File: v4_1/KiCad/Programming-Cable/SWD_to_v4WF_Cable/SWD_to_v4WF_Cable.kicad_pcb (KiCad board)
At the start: 2 copper layers, 60 x 20 mm, 19 parts, among them J1 Conn_01x05, J2 Conn_02x05_Odd_Even

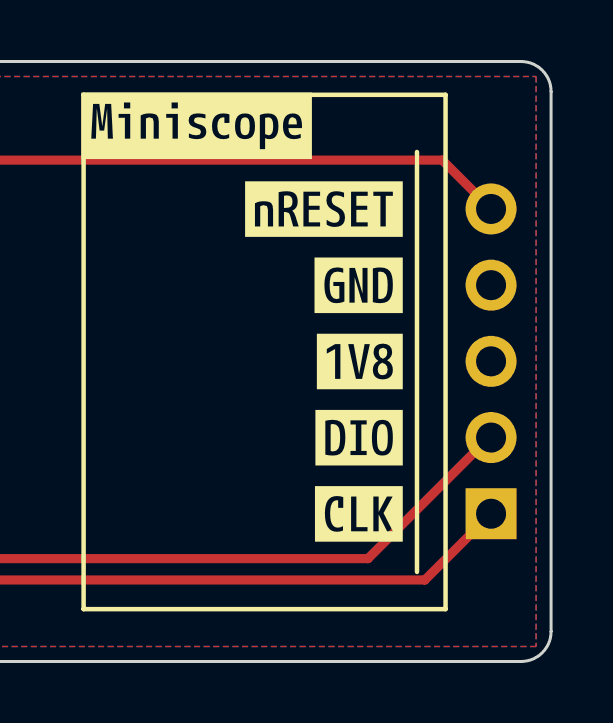
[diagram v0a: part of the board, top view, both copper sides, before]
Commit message: Modification to the Programming cable PCB and firmware
- Corrected the footprint and layout of the programming cable PCB. Switched from a 100 mil pogo pin connector to the correct size (50 mil)
- Cleaned and built the firmware for flashing to the MCU
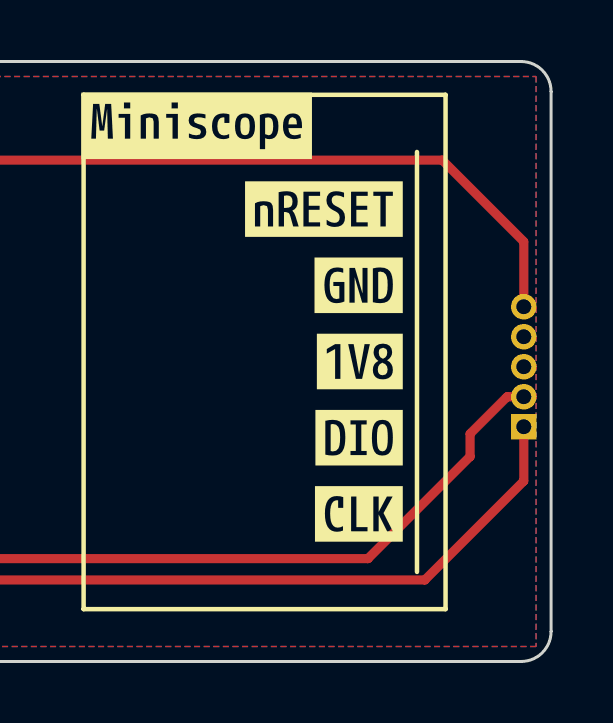
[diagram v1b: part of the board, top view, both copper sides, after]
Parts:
- J1: footprint Connector_PinHeader_2.54mm:PinHeader_1x05_P2.54mm_Vertical -> Connector_PinSocket_1.00mm:PinSocket_1x05_P1.00mm_Vertical
- moved J1 3.10 mm to (184.7, 61.5)
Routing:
- net /nRST: track 55.2 -> 59.0 mm
- net /SWDCLK: track 60.9 -> 64.2 mm
- net /SWDIO: track 56.3 -> 58.4 mm
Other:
- board text added: "SWD_to_v4WF_Cable v0.1 Karina Keus and Federico Sangiuliano Aharoni Lab, UCLA 08-31-2022 Rev1 12-3-2022"
- board text removed: "SWD_to_v4WF_Cable v0.1 Karina Keus and Federico Sangiuliano Aharoni Lab, UCLA 08-31-2022"
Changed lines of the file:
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@@
     )
   )
-  (footprint "Connector_PinHeader_2.54mm:PinHeader_1x05_P2.54mm_Vertical" (layer "B.Cu")
-    (at 183.6 64.425)
-    (descr "Through hole straight pin header, 1x05, 2.54mm pitch, single row")
-    (tags "Through hole pin header THT 1x05 2.54mm single row")
+  (footprint "Connector_PinSocket_1.00mm:PinSocket_1x05_P1.00mm_Vertical" (layer "B.Cu")
+    (at 184.69 61.525)
+    (descr "Through hole straight socket strip, 1x05, 1.00mm pitch, single row (https://gct.co/files/drawings/bc065.pdf), script generated")
+    (tags "Through hole socket strip THT 1x05 1.00mm single row")
     (property "Sheetfile" "SWD_to_v4WF_Cable.kicad_sch")
     (property "Sheetname" "")
     (attr through_hole)
-    (fp_text reference "J1" (at 0 2.33) (layer "B.SilkS") hide
+    (fp_text reference "J1" (at -0.29 2.25 180) (layer "B.SilkS")
       (effects (font (size 1 1) (thickness 0.15)) (justify mirror))
     )
-    (fp_text value "Conn_01x05" (at 0 -12.49) (layer "B.Fab")
+    (fp_text value "Conn_01x05" (at -0.29 -6.25 180) (layer "B.Fab")
       (effects (font (size 1 1) (thickness 0.15)) (justify mirror))
     )
-    (fp_text user "${REFERENCE}" (at 0 -5.08 90) (layer "B.Fab")
-      (effects (font (size 1 1) (thickness 0.15)) (justify mirror))
+    (fp_text user "${REFERENCE}" (at -0.29 -2 270) (layer "B.Fab")
+      (effects (font (size 0.9 0.9) (thickness 0.14)) (justify mirror))
     )
-    (fp_line (start 1.33 -1.27) (end 1.33 -11.49) (layer "B.SilkS") (width 0.12))
-    (fp_line (start -1.33 -1.27) (end 1.33 -1.27) (layer "B.SilkS") (width 0.12))
-    (fp_line (start -1.33 1.33) (end 0 1.33) (layer "B.SilkS") (width 0.12))
-    (fp_line (start -1.33 -1.27) (end -1.33 -11.49) (layer "B.SilkS") (width 0.12))
-    (fp_line (start -1.33 0) (end -1.33 1.33) (layer "B.SilkS") (width 0.12))
-    (fp_line (start -1.33 -11.49) (end 1.33 -11.49) (layer "B.SilkS") (width 0.12))
-    (fp_line (start -1.8 1.8) (end -1.8 -11.95) (layer "B.CrtYd") (width 0.05))
-    (fp_line (start 1.8 1.8) (end -1.8 1.8) (layer "B.CrtYd") (width 0.05))
-    (fp_line (start -1.8 -11.95) (end 1.8 -11.95) (layer "B.CrtYd") (width 0.05))
-    (fp_line (start 1.8 -11.95) (end 1.8 1.8) (layer "B.CrtYd") (width 0.05))
-    (fp_line (start -1.27 0.635) (end -0.635 1.27) (layer "B.Fab") (width 0.1))
-    (fp_line (start -1.27 -11.43) (end -1.27 0.635) (layer "B.Fab") (width 0.1))
-    (fp_line (start -0.635 1.27) (end 1.27 1.27) (layer "B.Fab") (width 0.1))
-    (fp_line (start 1.27 1.27) (end 1.27 -11.43) (layer "B.Fab") (width 0.1))
-    (fp_line (start 1.27 -11.43) (end -1.27 -11.43) (layer "B.Fab") (width 0.1))
-    (pad "1" thru_hole rect (at 0 0) (size 1.7 1.7) (drill 1) (layers *.Cu *.Mask)
+    (fp_line (start 0 0.81) (end 0.685 0.81) (layer "B.SilkS") (width 0.12))
+    (fp_line (start 0.52 -4.445898) (end 0.52 -4.81) (layer "B.SilkS") (width 0.12))
+    (fp_line (start 0.685 0.81) (end 0.685 0) (layer "B.SilkS") (width 0.12))
+    (fp_line (start -1.1 -4.81) (end 0.52 -4.81) (layer "B.SilkS") (width 0.12))
+    (fp_line (start 0.52 -3.445898) (end 0.52 -3.554102) (layer "B.SilkS") (width 0.12))
+    (fp_line (start -1.1 -0.5) (end -0.685 -0.5) (layer "B.SilkS") (width 0.12))
+    (fp_line (start 0.52 -1.445898) (end 0.52 -1.554102) (layer "B.SilkS") (width 0.12))
+    (fp_line (start 0.52 -2.445898) (end 0.52 -2.554102) (layer "B.SilkS") (width 0.12))
+    (fp_line (start -1.1 -0.5) (end -1.1 -4.81) (layer "B.SilkS") (width 0.12))
+    (fp_line (start -1.54 1.25) (end 0.96 1.25) (layer "B.CrtYd") (width 0.05))
+    (fp_line (start -1.54 -5.25) (end -1.54 1.25) (layer "B.CrtYd") (width 0.05))
+    (fp_line (start 0.96 1.25) (end 0.96 -5.25) (layer "B.CrtYd") (width 0.05))
+    (fp_line (start 0.96 -5.25) (end -1.54 -5.25) (layer "B.CrtYd") (width 0.05))
+    (fp_line (start 0.46 0.375) (end 0.46 -4.75) (layer "B.Fab") (width 0.1))
+    (fp_line (start 0.085 0.75) (end 0.46 0.375) (layer "B.Fab") (width 0.1))
+    (fp_line (start -1.04 -4.75) (end -1.04 0.75) (layer "B.Fab") (width 0.1))
+    (fp_line (start 0.46 -4.75) (end -1.04 -4.75) (layer "B.Fab") (width 0.1))
+    (fp_line (start -1.04 0.75) (end 0.085 0.75) (layer "B.Fab") (width 0.1))
+    (pad "1" thru_hole rect (at 0 0) (size 0.85 0.85) (drill 0.5) (layers *.Cu *.Mask)
       (net 1 "/SWDCLK") (pinfunction "Pin_1") (pintype "passive"))
-    (pad "2" thru_hole oval (at 0 -2.54) (size 1.7 1.7) (drill 1) (layers *.Cu *.Mask)
+    (pad "2" thru_hole oval (at 0 -1) (size 0.85 0.85) (drill 0.5) (layers *.Cu *.Mask)
       (net 2 "/SWDIO") (pinfunction "Pin_2") (pintype "passive"))
-    (pad "3" thru_hole oval (at 0 -5.08) (size 1.7 1.7) (drill 1) (layers *.Cu *.Mask)
+    (pad "3" thru_hole oval (at 0 -2) (size 0.85 0.85) (drill 0.5) (layers *.Cu *.Mask)
       (net 3 "+1V8") (pinfunction "Pin_3") (pintype "passive"))
-    (pad "4" thru_hole oval (at 0 -7.62) (size 1.7 1.7) (drill 1) (layers *.Cu *.Mask)
+    (pad "4" thru_hole oval (at 0 -3) (size 0.85 0.85) (drill 0.5) (layers *.Cu *.Mask)
       (net 4 "GND") (pinfunction "Pin_4") (pintype "passive"))
-    (pad "5" thru_hole oval (at 0 -10.16) (size 1.7 1.7) (drill 1) (layers *.Cu *.Mask)
+    (pad "5" thru_hole oval (at 0 -4) (size 0.85 0.85) (drill 0.5) (layers *.Cu *.Mask)
       (net 5 "/nRST") (pinfunction "Pin_5") (pintype "passive"))
-    (model "${KICAD6_3DMODEL_DIR}/Connector_PinHeader_2.54mm.3dshapes/PinHeader_1x05_P2.54mm_Vertical.wrl"
+    (model "${KICAD6_3DMODEL_DIR}/Connector_PinSocket_1.00mm.3dshapes/PinSocket_1x05_P1.00mm_Vertical.wrl"
       (offset (xyz 0 0 0))
       (scale (xyz 1 1 1))
@@
   (gr_line (start 185.6 68.35) (end 185.6 50.35) (layer "Edge.Cuts") (width 0.1))
   (gr_arc (start 126.87 69.35) (mid 125.971974 68.978026) (end 125.6 68.08) (layer "Edge.Cuts") (width 0.1))
-  (gr_text "SWD_to_v4WF_Cable v0.1\nKarina Keus and Federico Sangiuliano\nAharoni Lab, UCLA\n08-31-2022" (at 155.729991 59.349996) (layer "B.SilkS")
+  (gr_text "SWD_to_v4WF_Cable v0.1\nKarina Keus and Federico Sangiuliano\nAharoni Lab, UCLA\n08-31-2022\nRev1 12-3-2022" (at 155.729991 59.349996) (layer "B.SilkS")
     (effects (font (size 1 1) (thickness 0.15)) (justify mirror))
   )
+  (segment (start 128.1908 63.3048) (end 128.1908 65.1082) (width 0.3048) (layer "F.Cu") (net 1))
+  (segment (start 129.6106 61.885) (end 128.1908 63.3048) (width 0.3048) (layer "F.Cu") (net 1))
+  (segment (start 184.69 63.335) (end 184.69 61.525) (width 0.3048) (layer "F.Cu") (net 1))
   (segment (start 128.1908 65.1082) (end 129.7148 66.6322) (width 0.3048) (layer "F.Cu") (net 1))
+  (segment (start 181.3928 66.6322) (end 184.69 63.335) (width 0.3048) (layer "F.Cu") (net 1))
+  (segment (start 129.7148 66.6322) (end 181.3928 66.6322) (width 0.3048) (layer "F.Cu") (net 1))
   (segment (start 129.71 61.885) (end 129.6106 61.885) (width 0.3048) (layer "F.Cu") (net 1))
-  (segment (start 128.1908 63.3048) (end 128.1908 65.1082) (width 0.3048) (layer "F.Cu") (net 1))
-  (segment (start 181.3928 66.6322) (end 183.6 64.425) (width 0.3048) (layer "F.Cu") (net 1))
-  (segment (start 129.7148 66.6322) (end 181.3928 66.6322) (width 0.3048) (layer "F.Cu") (net 1))
-  (segment (start 129.6106 61.885) (end 128.1908 63.3048) (width 0.3048) (layer "F.Cu") (net 1))
+  (segment (start 182.9 61.761178) (end 184.136178 60.525) (width 0.3048) (layer "F.Cu") (net 2))
+  (segment (start 182.9 62.5198) (end 182.9 61.761178) (width 0.3048) (layer "F.Cu") (net 2))
+  (segment (start 184.136178 60.525) (end 184.69 60.525) (width 0.3048) (layer "F.Cu") (net 2))
   (segment (start 130.9385 65.921) (end 179.4988 65.921) (width 0.3048) (layer "F.Cu") (net 2))
+  (segment (start 179.4988 65.921) (end 182.9 62.5198) (width 0.3048) (layer "F.Cu") (net 2))
+  (segment (start 129.71 64.6925) (end 130.9385 65.921) (width 0.3048) (layer "F.Cu") (net 2))
   (segment (start 129.71 64.425) (end 129.71 64.6925) (width 0.3048) (layer "F.Cu") (net 2))
-  (segment (start 183.5348 61.885) (end 183.6 61.885) (width 0.3048) (layer "F.Cu") (net 2))
-  (segment (start 179.4988 65.921) (end 183.5348 61.885) (width 0.3048) (layer "F.Cu") (net 2))
-  (segment (start 129.71 64.6925) (end 130.9385 65.921) (width 0.3048) (layer "F.Cu") (net 2))
+  (segment (start 181.9718 52.6368) (end 184.69 55.355) (width 0.3048) (layer "F.Cu") (net 5))
+  (segment (start 184.69 55.355) (end 184.69 57.525) (width 0.3048) (layer "F.Cu") (net 5))
+  (segment (start 131.3382 52.6368) (end 181.9718 52.6368) (width 0.3048) (layer "F.Cu") (net 5))
   (segment (start 129.71 54.265) (end 131.3382 52.6368) (width 0.3048) (layer "F.Cu") (net 5))
-  (segment (start 131.3382 52.6368) (end 181.9718 52.6368) (width 0.3048) (layer "F.Cu") (net 5))
-  (segment (start 181.9718 52.6368) (end 183.6 54.265) (width 0.3048) (layer "F.Cu") (net 5))
   (zone (net 3) (net_name "+1V8") (layer "F.Cu") (hatch edge 0.508)
     (connect_pads (clearance 0.508))

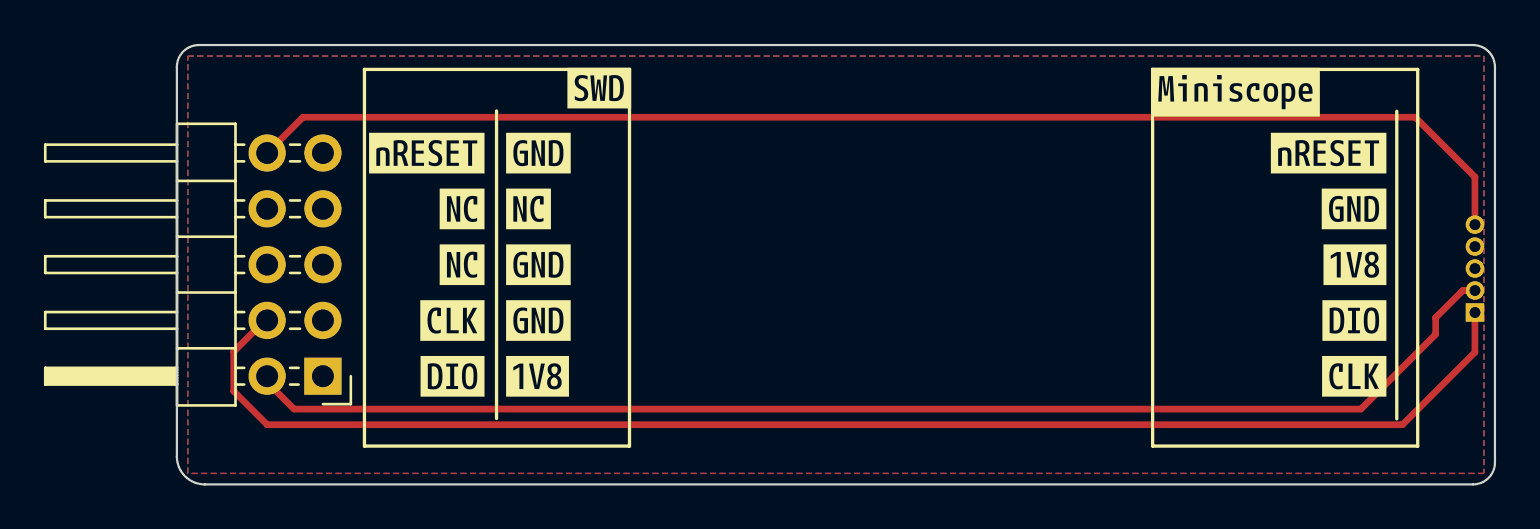
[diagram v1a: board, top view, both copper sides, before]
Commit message: Updates to the project
- Added code to test the functionality of the v4 WF and validate the design
- Fixed a bug that left the EWL run continuously even if it was not recording. Now once the recording ends the EWL goes to sleep mode
- Modified the threshold for which the recording stops once the battery ADC reading reaches certain value
- Fixed a typo on the jupyter notebook name
- Fixed the programming cable by changing the target programming pins footprint
- Added a folder with a KiCAD project for the EWL cable
- For both things I generated new gerbers, which I checked using the gerber viewer
- Not uploaded to the repo due to size constrains: videos demonstrating that the Miniscope can record continuously for over 20 minutes

To do (in the short term):

- Add requirements to create a conda environment for easier use of the DAQ notebook
- Clean a bit more the code
- Add to the documentation the fix we applied to fix the bug that prevented the Miniscope to not run on Release mode
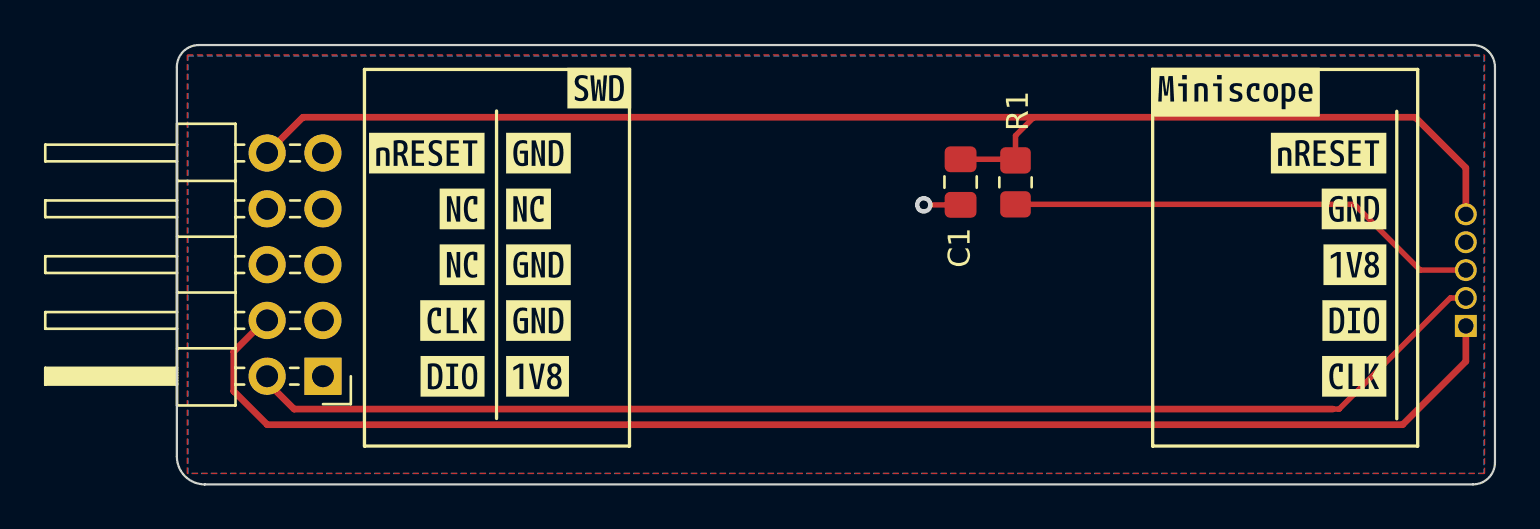
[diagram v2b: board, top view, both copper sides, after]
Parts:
- added C1: 1u, Capacitor_SMD:C_0805_2012Metric_Pad1.18x1.45mm_HandSolder, F.Cu at (161.3, 55.6)
- added R1: 10k, Resistor_SMD:R_0805_2012Metric_Pad1.20x1.40mm_HandSolder, F.Cu at (163.8, 55.6)
- J1: footprint Connector_PinSocket_1.00mm:PinSocket_1x05_P1.00mm_Vertical -> Connector_PinSocket_1.27mm:PinSocket_1x05_P1.27mm_Vertical
- moved J1 0.74 mm to (184.3, 62.1)
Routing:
- net +1V8: track 0.00 -> 21.7 mm
- net /nRST: track 59.0 -> 63.1 mm
- net GND: track 0.00 -> 1.68 mm, vias 0 -> 1
- net /SWDIO: track 58.4 -> 57.4 mm
- net /SWDCLK: track 64.2 -> 63.4 mm
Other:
- board text added: "SWD_to_v4WF_Cable v0.1 Karina Keus and Federico Sangiuliano Aharoni Lab, UCLA 08-31-2022 Rev1 2-6-2023"
- board text removed: "SWD_to_v4WF_Cable v0.1 Karina Keus and Federico Sangiuliano Aharoni Lab, UCLA 08-31-2022 Rev1 12-3-2022"
